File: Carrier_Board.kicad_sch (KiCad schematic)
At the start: 6 parts

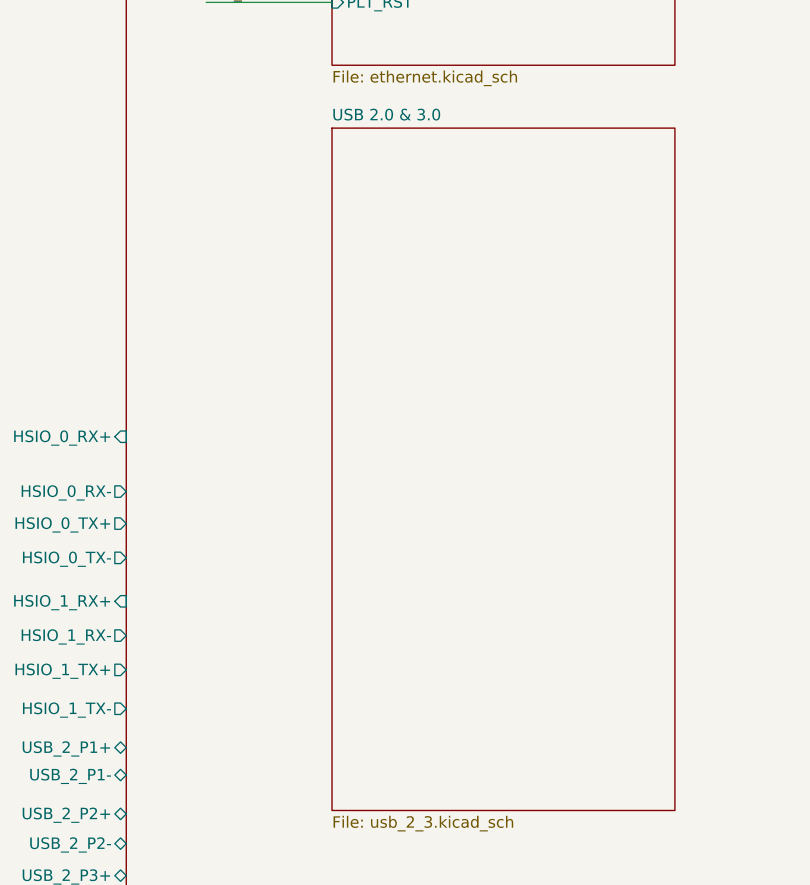
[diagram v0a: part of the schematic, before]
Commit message: Fixed the labels to the netlabels in the USB schema sheet
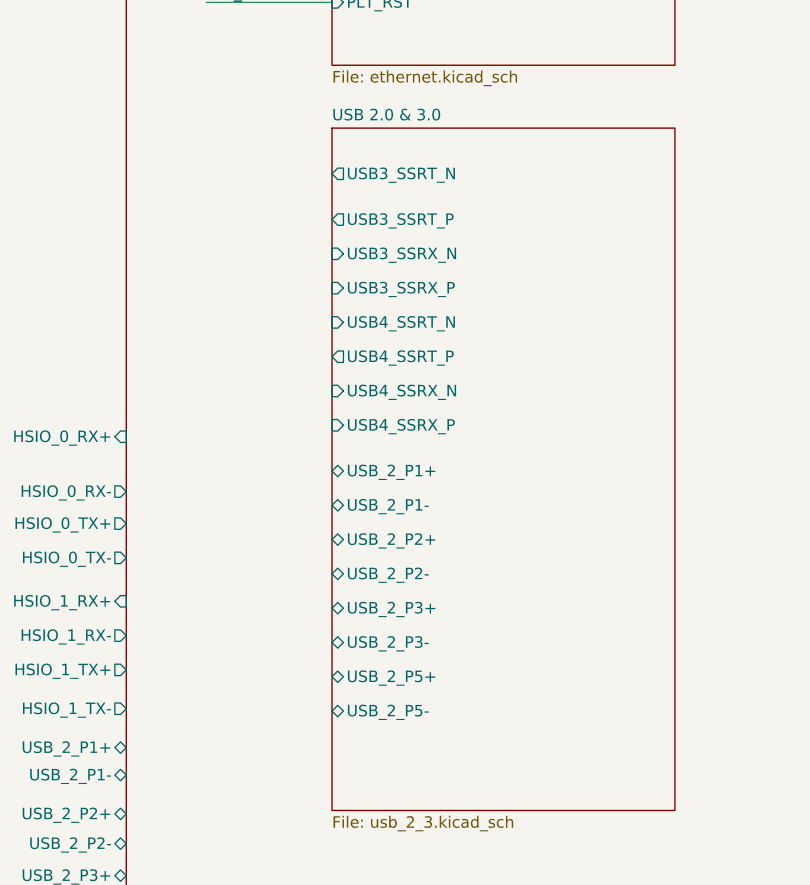
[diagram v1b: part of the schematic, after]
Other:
- sheet USB 2.0 & 3.0 ports: added USB3_SSRT_N, USB3_SSRT_P, USB3_SSRX_N, USB3_SSRX_P, USB4_SSRT_N, USB4_SSRT_P, USB4_SSRX_N, USB4_SSRX_P, USB_2_P1+, USB_2_P1-, USB_2_P2+, USB_2_P2-, USB_2_P3+, USB_2_P3-, USB_2_P5+, USB_2_P5-; removed none
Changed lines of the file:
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@@
+			)
+		)
+		(pin "USB3_SSRT_N" output
+			(at 325.12 139.7 180)
+			(effects
+				(font
+					(size 1.27 1.27)
+				)
+				(justify left)
+			)
+		)
+		(pin "USB3_SSRT_P" output
+			(at 325.12 144.78 180)
+			(effects
+				(font
+					(size 1.27 1.27)
+				)
+				(justify left)
+			)
+		)
+		(pin "USB3_SSRX_N" input
+			(at 325.12 148.59 180)
+			(effects
+				(font
+					(size 1.27 1.27)
+				)
+				(justify left)
+			)
+		)
+		(pin "USB3_SSRX_P" input
+			(at 325.12 152.4 180)
+			(effects
+				(font
+					(size 1.27 1.27)
+				)
+				(justify left)
+			)
+		)
+		(pin "USB4_SSRT_N" input
+			(at 325.12 156.21 180)
+			(effects
+				(font
+					(size 1.27 1.27)
+				)
+				(justify left)
+			)
+		)
+		(pin "USB4_SSRT_P" output
+			(at 325.12 160.02 180)
+			(effects
+				(font
+					(size 1.27 1.27)
+				)
+				(justify left)
+			)
+		)
+		(pin "USB4_SSRX_N" input
+			(at 325.12 163.83 180)
+			(effects
+				(font
+					(size 1.27 1.27)
+				)
+				(justify left)
+			)
+		)
+		(pin "USB4_SSRX_P" input
+			(at 325.12 167.64 180)
+			(effects
+				(font
+					(size 1.27 1.27)
+				)
+				(justify left)
+			)
+		)
+		(pin "USB_2_P1+" bidirectional
+			(at 325.12 172.72 180)
+			(effects
+				(font
+					(size 1.27 1.27)
+				)
+				(justify left)
+			)
+		)
+		(pin "USB_2_P1-" bidirectional
+			(at 325.12 176.53 180)
+			(effects
+				(font
+					(size 1.27 1.27)
+				)
+				(justify left)
+			)
+		)
+		(pin "USB_2_P2+" bidirectional
+			(at 325.12 180.34 180)
+			(effects
+				(font
+					(size 1.27 1.27)
+				)
+				(justify left)
+			)
+		)
+		(pin "USB_2_P2-" bidirectional
+			(at 325.12 184.15 180)
+			(effects
+				(font
+					(size 1.27 1.27)
+				)
+				(justify left)
+			)
+		)
+		(pin "USB_2_P3+" bidirectional
+			(at 325.12 187.96 180)
+			(effects
+				(font
+					(size 1.27 1.27)
+				)
+				(justify left)
+			)
+		)
+		(pin "USB_2_P3-" bidirectional
+			(at 325.12 191.77 180)
+			(effects
+				(font
+					(size 1.27 1.27)
+				)
+				(justify left)
+			)
+		)
+		(pin "USB_2_P5+" bidirectional
+			(at 325.12 195.58 180)
+			(effects
+				(font
+					(size 1.27 1.27)
+				)
+				(justify left)
+			)
+		)
+		(pin "USB_2_P5-" bidirectional
+			(at 325.12 199.39 180)
+			(effects
+				(font
+					(size 1.27 1.27)
+				)
+				(justify left)
 			)
 		)

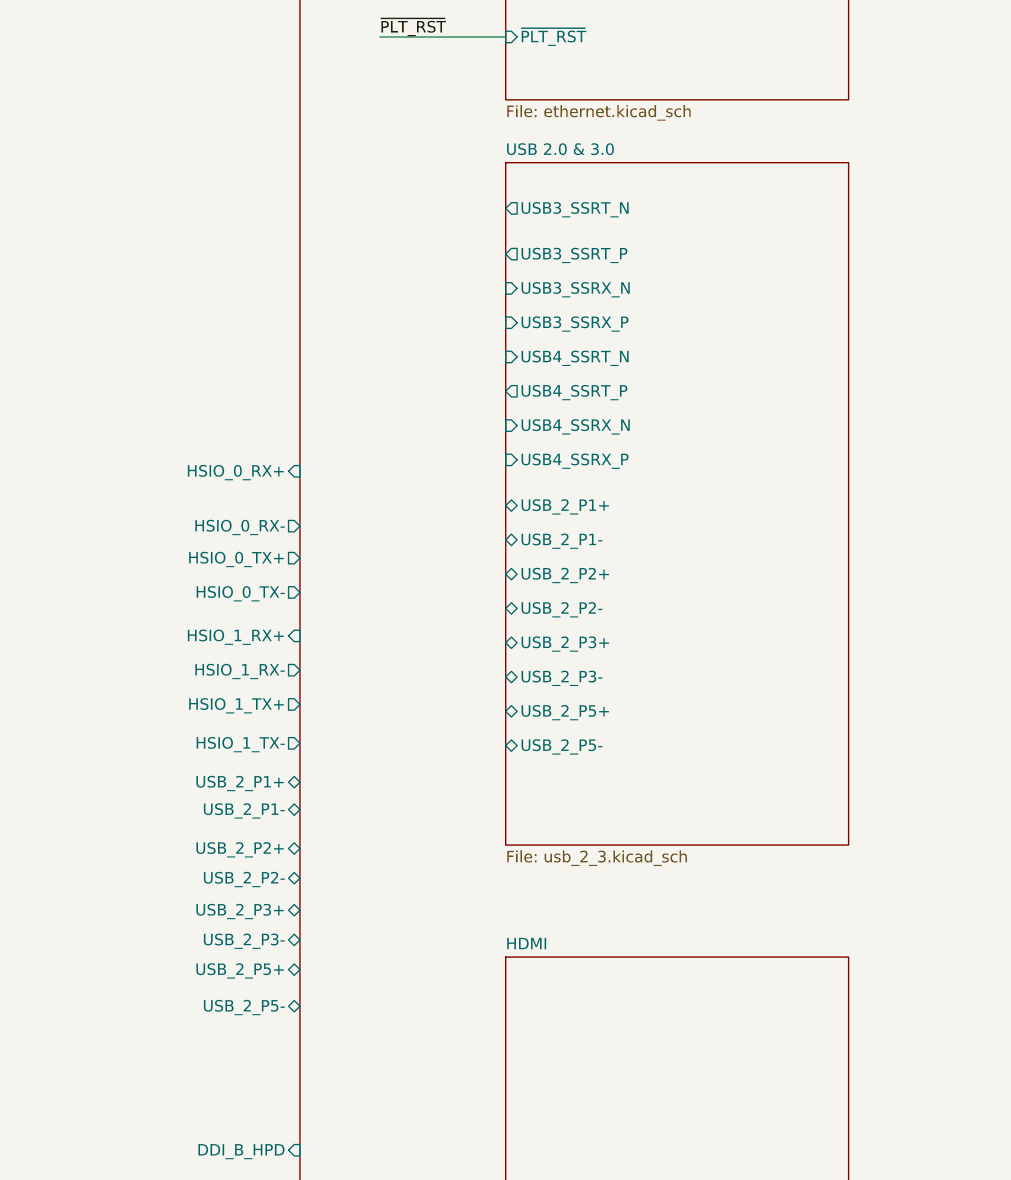
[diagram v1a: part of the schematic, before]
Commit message: Connected the usb sheets together in the the roor sheet
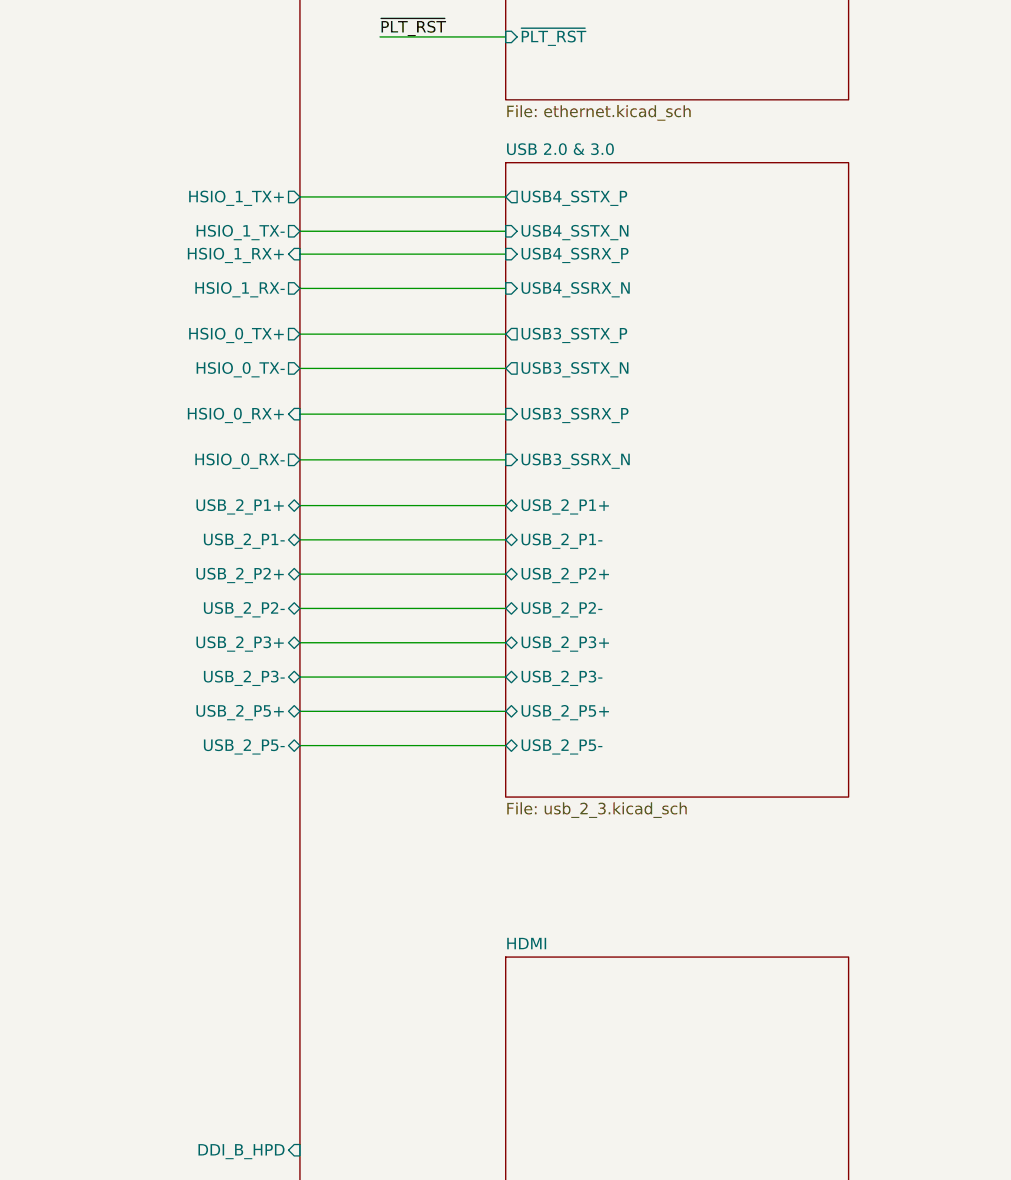
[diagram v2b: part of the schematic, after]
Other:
- sheet USB 2.0 & 3.0 ports: added USB3_SSTX_N, USB3_SSTX_P, USB4_SSTX_N, USB4_SSTX_P; removed USB3_SSRT_N, USB3_SSRT_P, USB4_SSRT_N, USB4_SSRT_P
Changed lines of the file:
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@@
 	(wire
 		(pts
+			(xy 302.26 199.39) (xy 325.12 199.39)
+		)
+		(stroke
+			(width 0)
+			(type default)
+		)
+	)
+	(wire
+		(pts
 			(xy 175.26 297.18) (xy 203.2 297.18)
 		)
@@
 	(wire
 		(pts
+			(xy 302.26 172.72) (xy 325.12 172.72)
+		)
+		(stroke
+			(width 0)
+			(type default)
+		)
+	)
+	(wire
+		(pts
+			(xy 302.26 176.53) (xy 325.12 176.53)
+		)
+		(stroke
+			(width 0)
+			(type default)
+		)
+	)
+	(wire
+		(pts
 			(xy 172.72 83.82) (xy 203.2 83.82)
 		)
@@
 	(wire
 		(pts
+			(xy 302.26 142.24) (xy 325.12 142.24)
+		)
+		(stroke
+			(width 0)
+			(type default)
+		)
+	)
+	(wire
+		(pts
+			(xy 302.26 191.77) (xy 325.12 191.77)
+		)
+		(stroke
+			(width 0)
+			(type default)
+		)
+	)
+	(wire
+		(pts
 			(xy 175.26 223.52) (xy 203.2 223.52)
 		)
@@
 	(wire
 		(pts
+			(xy 302.26 167.64) (xy 325.12 167.64)
+		)
+		(stroke
+			(width 0)
+			(type default)
+		)
+	)
+	(wire
+		(pts
+			(xy 302.26 153.67) (xy 325.12 153.67)
+		)
+		(stroke
+			(width 0)
+			(type default)
+		)
+	)
+	(wire
+		(pts
 			(xy 175.26 322.58) (xy 203.2 322.58)
 		)
@@
 	(wire
 		(pts
+			(xy 302.26 184.15) (xy 325.12 184.15)
+		)
+		(stroke
+			(width 0)
+			(type default)
+		)
+	)
+	(wire
+		(pts
+			(xy 302.26 187.96) (xy 325.12 187.96)
+		)
+		(stroke
+			(width 0)
+			(type default)
+		)
+	)
+	(wire
+		(pts
+			(xy 302.26 157.48) (xy 325.12 157.48)
+		)
+		(stroke
+			(width 0)
+			(type default)
+		)
+	)
+	(wire
+		(pts
 			(xy 175.26 127) (xy 203.2 127)
 		)
@@
 	(wire
 		(pts
+			(xy 302.26 195.58) (xy 325.12 195.58)
+		)
+		(stroke
+			(width 0)
+			(type default)
+		)
+	)
+	(wire
+		(pts
 			(xy 175.26 332.74) (xy 203.2 332.74)
 		)
@@
 	(wire
 		(pts
+			(xy 302.26 144.78) (xy 325.12 144.78)
+		)
+		(stroke
+			(width 0)
+			(type default)
+		)
+	)
+	(wire
+		(pts
 			(xy 175.26 146.05) (xy 203.2 146.05)
 		)
@@
 	(wire
 		(pts
+			(xy 302.26 138.43) (xy 325.12 138.43)
+		)
+		(stroke
+			(width 0)
+			(type default)
+		)
+	)
+	(wire
+		(pts
 			(xy 175.26 204.47) (xy 203.2 204.47)
 		)
@@
 	(wire
 		(pts
+			(xy 302.26 180.34) (xy 325.12 180.34)
+		)
+		(stroke
+			(width 0)
+			(type default)
+		)
+	)
+	(wire
+		(pts
+			(xy 302.26 148.59) (xy 325.12 148.59)
+		)
+		(stroke
+			(width 0)
+			(type default)
+		)
+	)
+	(wire
+		(pts
 			(xy 175.26 325.12) (xy 203.2 325.12)
 		)
@@
 	(wire
 		(pts
+			(xy 302.26 162.56) (xy 325.12 162.56)
+		)
+		(stroke
+			(width 0)
+			(type default)
+		)
+	)
+	(wire
+		(pts
 			(xy 175.26 312.42) (xy 203.2 312.42)
 		)
@@
 		)
 		(pin "HSIO_0_RX+" input
-			(at 302.26 168.91 0)
+			(at 302.26 162.56 0)
 			(effects
 				(font
@@
 		)
 		(pin "HSIO_0_RX-" output
-			(at 302.26 175.006 0)
+			(at 302.26 167.64 0)
 			(effects
 				(font
@@
 		)
 		(pin "HSIO_0_TX+" output
-			(at 302.26 178.562 0)
+			(at 302.26 153.67 0)
 			(effects
 				(font
@@
 		)
 		(pin "HSIO_0_TX-" output
-			(at 302.26 182.372 0)
+			(at 302.26 157.48 0)
 			(effects
 				(font
@@
 		)
 		(pin "HSIO_1_RX+" input
-			(at 302.26 187.198 0)
+			(at 302.26 144.78 0)
 			(effects
 				(font
@@
 		)
 		(pin "HSIO_1_RX-" output
-			(at 302.26 191.008 0)
+			(at 302.26 148.59 0)
 			(effects
 				(font
@@
 		)
 		(pin "HSIO_1_TX+" output
-			(at 302.26 194.818 0)
+			(at 302.26 138.43 0)
 			(effects
 				(font
@@
 		)
 		(pin "HSIO_1_TX-" output
-			(at 302.26 199.136 0)
+			(at 302.26 142.24 0)
 			(effects
 				(font
@@
 		)
 		(pin "USB_2_P1+" bidirectional
-			(at 302.26 203.454 0)
+			(at 302.26 172.72 0)
 			(effects
 				(font
@@
 		)
 		(pin "USB_2_P1-" bidirectional
-			(at 302.26 206.502 0)
+			(at 302.26 176.53 0)
 			(effects
 				(font
@@
 		)
 		(pin "USB_2_P2+" bidirectional
-			(at 302.26 210.82 0)
+			(at 302.26 180.34 0)
 			(effects
 				(font
@@
 		)
 		(pin "USB_2_P2-" bidirectional
-			(at 302.26 214.122 0)
+			(at 302.26 184.15 0)
 			(effects
 				(font
@@
 		)
 		(pin "USB_2_P3+" bidirectional
-			(at 302.26 217.678 0)
+			(at 302.26 187.96 0)
 			(effects
 				(font
@@
 		)
 		(pin "USB_2_P3-" bidirectional
-			(at 302.26 220.98 0)
+			(at 302.26 191.77 0)
 			(effects
 				(font
@@
 		)
 		(pin "USB_2_P5+" bidirectional
-			(at 302.26 224.282 0)
+			(at 302.26 195.58 0)
 			(effects
 				(font
@@
 		)
 		(pin "USB_2_P5-" bidirectional
-			(at 302.26 228.346 0)
+			(at 302.26 199.39 0)
 			(effects
 				(font
@@
 	(sheet
 		(at 325.12 134.62)
-		(size 38.1 75.819)
+		(size 38.1 70.485)
 		(exclude_from_sim no)
 		(in_bom yes)
@@
 		)
 		(property "Sheetfile" "usb_2_3.kicad_sch"
-			(at 325.12 211.0236 0)
+			(at 325.12 205.6896 0)
 			(show_name no)
 			(do_not_autoplace no)
@@
 			)
 		)
-		(pin "USB3_SSRT_N" output
-			(at 325.12 139.7 180)
+		(pin "USB4_SSRX_N" input
+			(at 325.12 148.59 180)
 			(effects
 				(font
@@
 			)
 		)
-		(pin "USB3_SSRT_P" output
+		(pin "USB4_SSRX_P" input
 			(at 325.12 144.78 180)
 			(effects
@@
 			)
 		)
-		(pin "USB3_SSRX_N" input
-			(at 325.12 148.59 180)
+		(pin "USB_2_P1+" bidirectional
+			(at 325.12 172.72 180)
 			(effects
 				(font
@@
 			)
 		)
-		(pin "USB3_SSRX_P" input
-			(at 325.12 152.4 180)
+		(pin "USB_2_P1-" bidirectional
+			(at 325.12 176.53 180)
 			(effects
 				(font
@@
 			)
 		)
-		(pin "USB4_SSRT_N" input
-			(at 325.12 156.21 180)
+		(pin "USB_2_P2+" bidirectional
+			(at 325.12 180.34 180)
 			(effects
 				(font
@@
 			)
 		)
-		(pin "USB4_SSRT_P" output
-			(at 325.12 160.02 180)
+		(pin "USB_2_P2-" bidirectional
+			(at 325.12 184.15 180)
 			(effects
 				(font
@@
 			)
 		)
-		(pin "USB4_SSRX_N" input
-			(at 325.12 163.83 180)
+		(pin "USB_2_P3+" bidirectional
+			(at 325.12 187.96 180)
 			(effects
 				(font
@@
 			)
 		)
-		(pin "USB4_SSRX_P" input
-			(at 325.12 167.64 180)
+		(pin "USB_2_P3-" bidirectional
+			(at 325.12 191.77 180)
 			(effects
 				(font
@@
 			)
 		)
-		(pin "USB_2_P1+" bidirectional
-			(at 325.12 172.72 180)
+		(pin "USB_2_P5+" bidirectional
+			(at 325.12 195.58 180)
 			(effects
 				(font
@@
 			)
 		)
-		(pin "USB_2_P1-" bidirectional
-			(at 325.12 176.53 180)
+		(pin "USB_2_P5-" bidirectional
+			(at 325.12 199.39 180)
 			(effects
 				(font
@@
 			)
 		)
-		(pin "USB_2_P2+" bidirectional
-			(at 325.12 180.34 180)
+		(pin "USB3_SSTX_N" output
+			(at 325.12 157.48 180)
 			(effects
 				(font
@@
 			)
 		)
-		(pin "USB_2_P2-" bidirectional
-			(at 325.12 184.15 180)
+		(pin "USB3_SSTX_P" output
+			(at 325.12 153.67 180)
 			(effects
 				(font
@@
 			)
 		)
-		(pin "USB_2_P3+" bidirectional
-			(at 325.12 187.96 180)
+		(pin "USB4_SSTX_N" input
+			(at 325.12 142.24 180)
 			(effects
 				(font
@@
 			)
 		)
-		(pin "USB_2_P3-" bidirectional
-			(at 325.12 191.77 180)
+		(pin "USB4_SSTX_P" output
+			(at 325.12 138.43 180)
 			(effects
 				(font
@@
 			)
 		)
-		(pin "USB_2_P5+" bidirectional
-			(at 325.12 195.58 180)
+		(pin "USB3_SSRX_N" input
+			(at 325.12 167.64 180)
 			(effects
 				(font
@@
 			)
 		)
-		(pin "USB_2_P5-" bidirectional
-			(at 325.12 199.39 180)
+		(pin "USB3_SSRX_P" input
+			(at 325.12 162.56 180)
 			(effects
 				(font

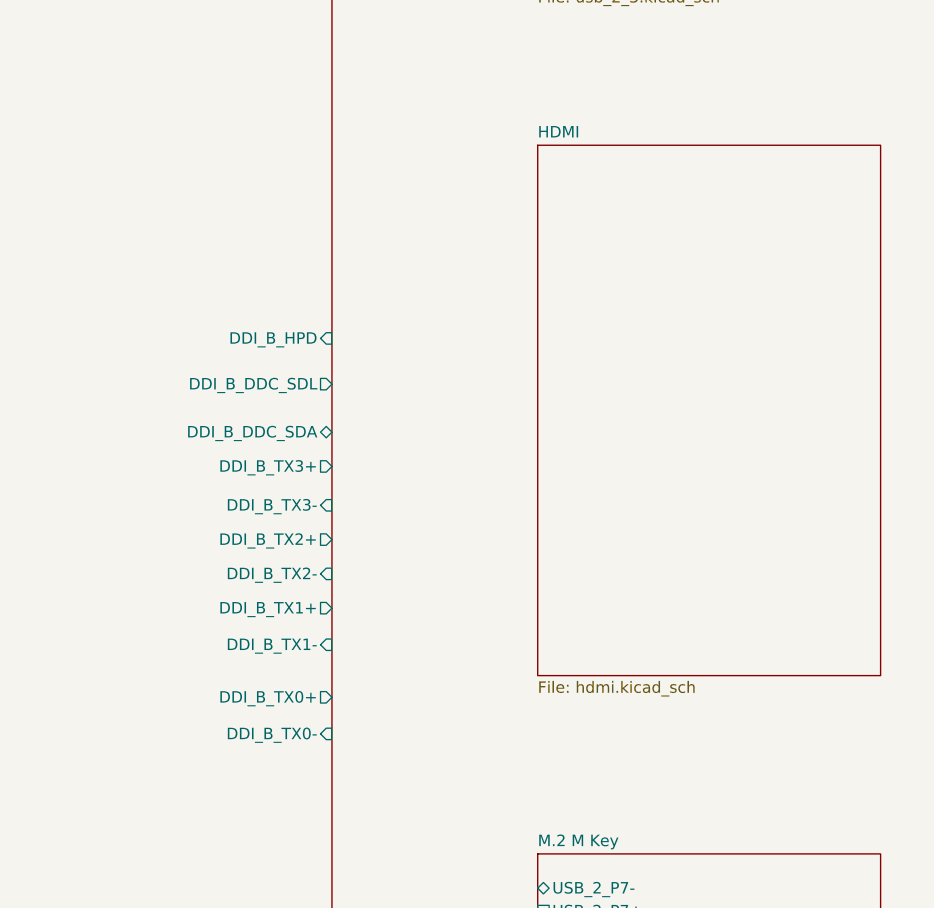
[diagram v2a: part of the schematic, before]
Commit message: Finished the HDMI circuit and connected labels to Mu model in root sheet
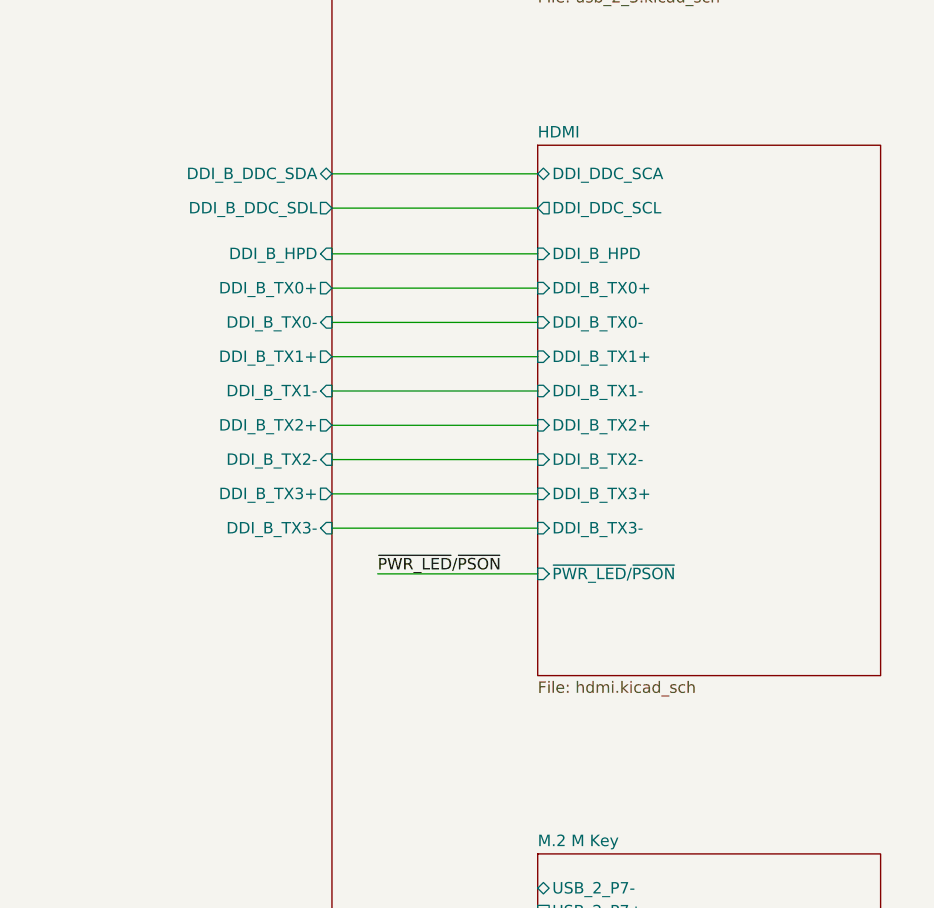
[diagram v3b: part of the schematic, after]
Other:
- sheet HDMI ports: added DDI_B_HPD, DDI_B_TX0+, DDI_B_TX0-, DDI_B_TX1+, DDI_B_TX1-, DDI_B_TX2+, DDI_B_TX2-, DDI_B_TX3+, DDI_B_TX3-, DDI_DDC_SCA, DDI_DDC_SCL, ~{PWR_LED}/~{PSON}; removed none
